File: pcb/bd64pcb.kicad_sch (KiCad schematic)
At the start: 229 parts, among them J1 USB_C_Receptacle_USB2.0, SW1 SW_Push, U1 ATmega32U4-MU, U3 IS31FL3733-QF, Y1 16MHz

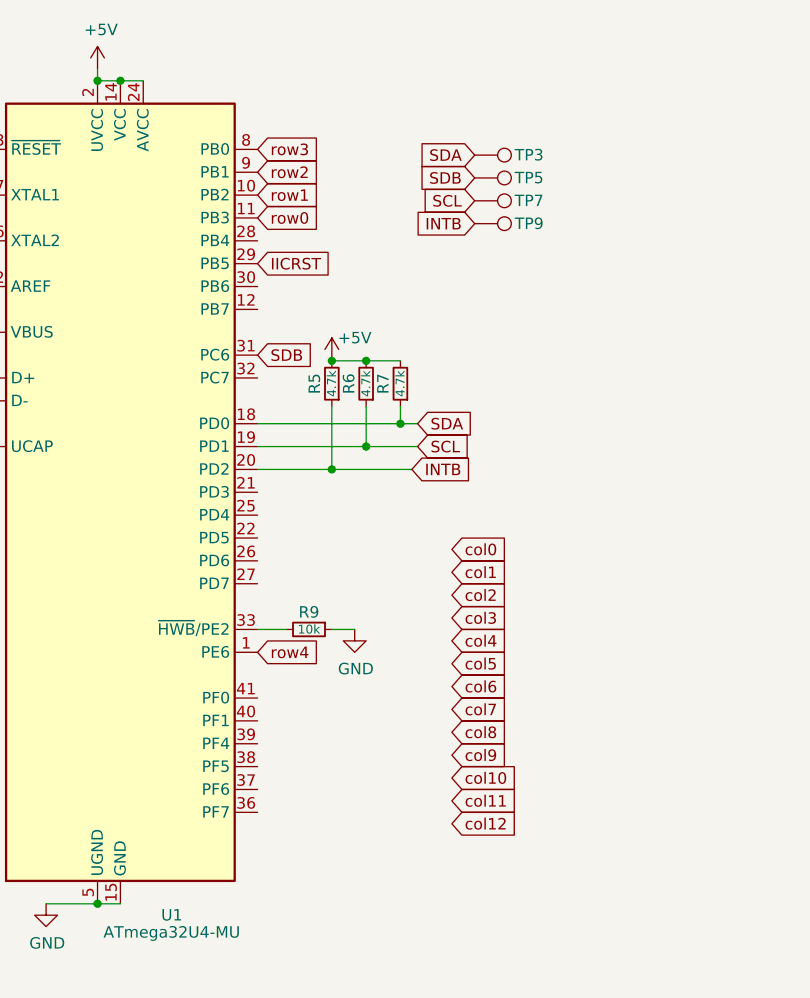
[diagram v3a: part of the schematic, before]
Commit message: rows, cols, and i2c routed
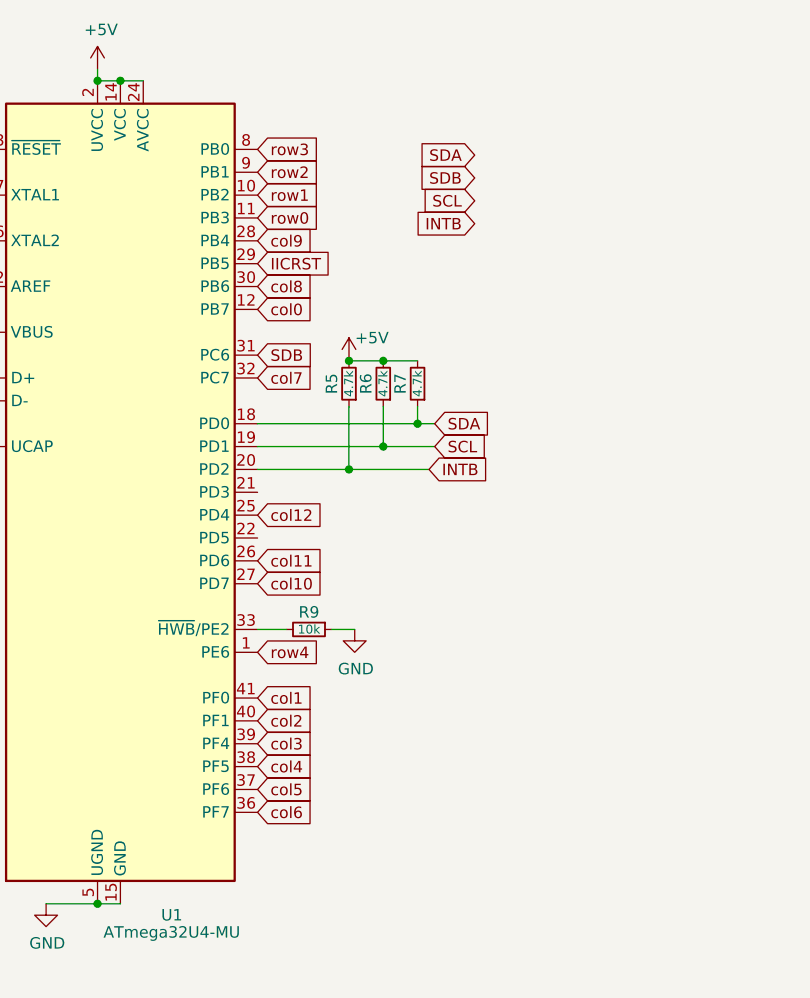
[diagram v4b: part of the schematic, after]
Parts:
- removed TP3, TP5, TP7, TP9: TestPoint, TestPoint:TestPoint_Plated_Hole_D2.0mm, symbol Connector:TestPoint
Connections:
- net col0: now also U1.12 (PB7)
- net col1: now also U1.41 (PF0)
- net col10: now also U1.27 (PD7)
- net col11: now also U1.26 (PD6)
- net col12: now also U1.25 (PD4)
- net col2: now also U1.40 (PF1)
- net col3: now also U1.39 (PF4)
- net col4: now also U1.38 (PF5)
- net col5: now also U1.37 (PF6)
- net col6: now also U1.36 (PF7)
- net col7: now also U1.32 (PC7)
- net col8: now also U1.30 (PB6)
- net col9: now also U1.28 (PB4)
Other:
- moved on the sheet: R5, R6, R7

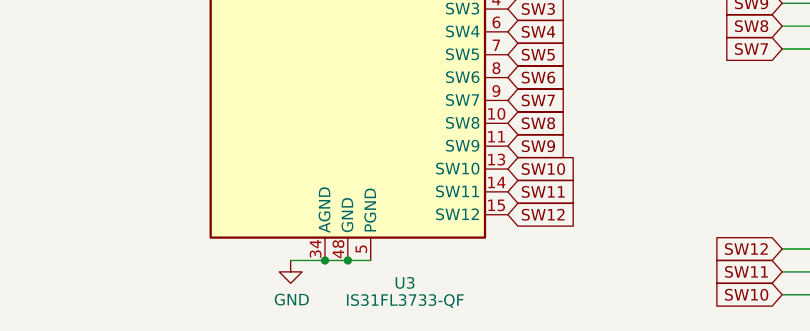
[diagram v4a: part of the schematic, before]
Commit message: decluttering silk labels with arrows
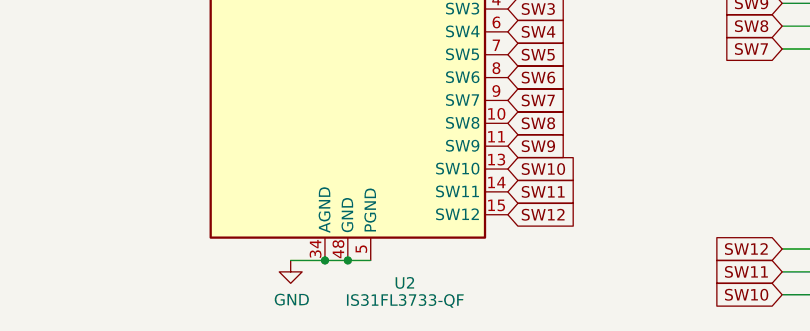
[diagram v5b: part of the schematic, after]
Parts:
- renumbered U3 to U2
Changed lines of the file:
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@@
   (symbol (lib_id "Driver_LED:IS31FL3733-QF") (at 66.675 213.995 0) (unit 1)
     (in_bom yes) (on_board yes)
-    (property "Reference" "U3" (id 0) (at 73.025 257.175 0))
+    (property "Reference" "U2" (id 0) (at 73.025 257.175 0))
     (property "Value" "IS31FL3733-QF" (id 1) (at 73.025 259.08 0))
     (property "Footprint" "Package_DFN_QFN:QFN-48-1EP_6x6mm_P0.4mm_EP4.2x4.2mm" (id 2) (at 66.675 213.995 0)
@@
     )
     (path "/00000000-0000-0000-0000-000062c2eea5"
-      (reference "U3") (unit 1) (value "IS31FL3733-QF") (footprint "Package_DFN_QFN:QFN-48-1EP_6x6mm_P0.4mm_EP4.2x4.2mm")
+      (reference "U2") (unit 1) (value "IS31FL3733-QF") (footprint "Package_DFN_QFN:QFN-48-1EP_6x6mm_P0.4mm_EP4.2x4.2mm")
     )
     (path "/00000000-0000-0000-0000-00006298f3ae"

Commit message: reorg
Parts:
- added J2, J3: Conn_01x04, Connector_JST:JST_SUR_SM04B-SURS-TF_1x04-1MP_P0.80mm_Horizontal, symbol Connector_Generic:Conn_01x04
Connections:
- net +5V: now also J2.2 (Pin_2), J3.2 (Pin_2)
- net GND: now also J2.1 (Pin_1), J2.MP, J3.1 (Pin_1), J3.MP
- net SCL: now also J2.4 (Pin_4), J3.4 (Pin_4)
- net SDA: now also J2.3 (Pin_3), J3.3 (Pin_3)

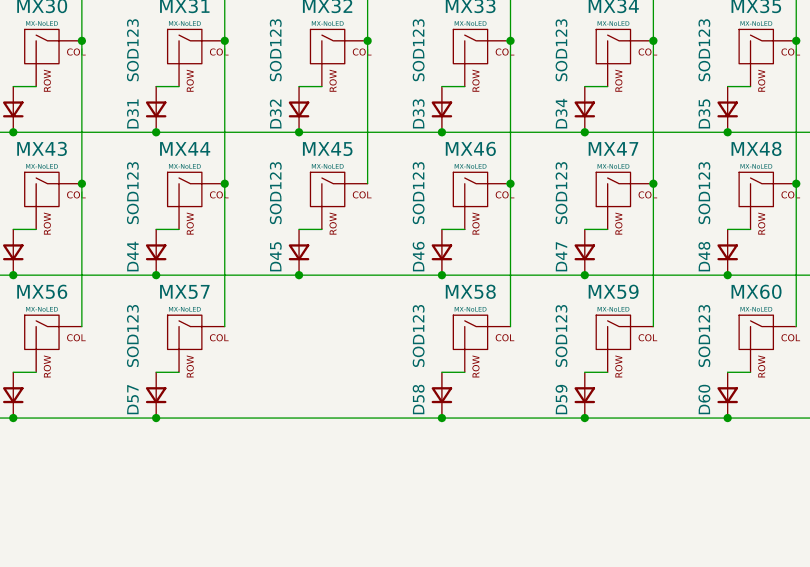
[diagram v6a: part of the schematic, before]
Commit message: update sch footprints, add 6.25 space opt
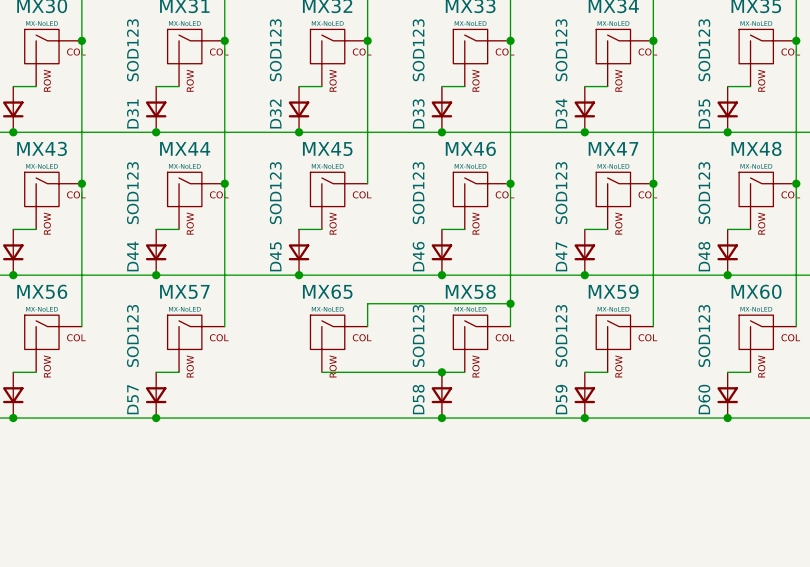
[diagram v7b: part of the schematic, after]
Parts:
- added MX65: MX-NoLED, MX_Only:MXOnly-6.25U-ReversedStabilizers-NoLED, symbol MX_Alps_Hybrid:MX-NoLED
- J1: footprint Connector_USB:USB_C_Receptacle_GCT_USB4085 -> Connector_USB:USB_C_Receptacle_HRO_TYPE-C-31-M-12
- MX10, MX11, MX12, MX13, MX14, MX16, MX17, MX18, MX19, MX20, MX21, MX22, MX23, MX24, MX25, MX26, MX29, MX30, MX31, MX32, MX33, MX34, MX35, MX36, MX37, MX38, MX39, MX4, MX42, MX43, MX44, MX45, MX46, MX47, MX48, MX49, MX5, MX50, MX51, MX52, MX58, MX59, MX6, MX7, MX8, MX9: footprint MX_Alps_Hybrid:MX-1U-NoLED -> MX_Only:MXOnly-1U-NoLED
- MX15, MX53, MX54, MX55, MX61, MX62, MX63, MX64: footprint MX_Alps_Hybrid:MX-1.25U-NoLED -> MX_Only:MXOnly-1.25U-NoLED
- MX27, MX41: footprint MX_Alps_Hybrid:MX-1.75U-NoLED -> MX_Only:MXOnly-1.75U-NoLED
- MX28, MX40, MX56, MX57, MX60: footprint MX_Alps_Hybrid:MX-1.5U-NoLED -> MX_Only:MXOnly-1.5U-NoLED
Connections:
- net col5: now also MX65.1 (COL)
- net at D58.2 (A), MX58.2 (ROW): now also MX65.2 (ROW)

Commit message: scrapping alt space layout
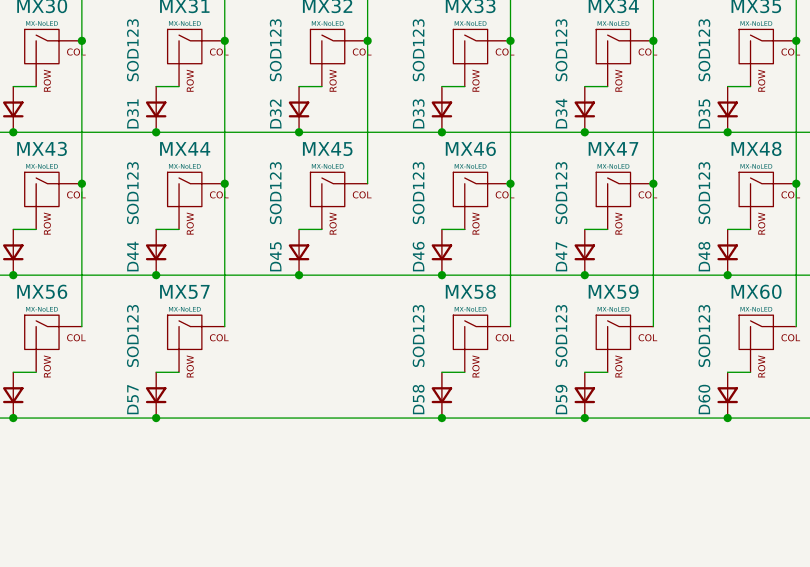
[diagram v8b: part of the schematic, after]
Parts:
- removed MX65: MX-NoLED, MX_Only:MXOnly-6.25U-ReversedStabilizers-NoLED, symbol MX_Alps_Hybrid:MX-NoLED
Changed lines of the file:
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@@
   (junction (at 357.505 60.325) (diameter 0) (color 0 0 0 0)
   )
-  (junction (at 309.88 118.745) (diameter 0) (color 0 0 0 0)
-  )
   (junction (at 262.255 60.325) (diameter 0) (color 0 0 0 0)
   )
@@
   (junction (at 309.88 123.825) (diameter 0) (color 0 0 0 0)
   )
-  (junction (at 317.5 111.125) (diameter 0) (color 0 0 0 0)
-  )
   (junction (at 301.625 171.45) (diameter 0) (color 0 0 0 0)
   )
@@
     (stroke (width 0) (type default) (color 0 0 0 0))
   )
-  (wire (pts (xy 301.625 111.125) (xy 317.5 111.125))
-    (stroke (width 0) (type default) (color 0 0 0 0))
-  )
   (wire (pts (xy 248.92 55.245) (xy 246.38 55.245))
     (stroke (width 0) (type default) (color 0 0 0 0))
@@
     (stroke (width 0) (type default) (color 0 0 0 0))
   )
-  (wire (pts (xy 317.5 113.665) (xy 317.5 111.125))
+  (wire (pts (xy 317.5 97.79) (xy 317.5 113.665))
     (stroke (width 0) (type default) (color 0 0 0 0))
   )
@@
     (stroke (width 0) (type default) (color 0 0 0 0))
   )
-  (wire (pts (xy 301.625 113.665) (xy 301.625 111.125))
-    (stroke (width 0) (type default) (color 0 0 0 0))
-  )
   (wire (pts (xy 81.28 68.58) (xy 77.47 68.58))
     (stroke (width 0) (type default) (color 0 0 0 0))
@@
     (stroke (width 0) (type default) (color 0 0 0 0))
   )
-  (wire (pts (xy 296.545 118.745) (xy 309.88 118.745))
-    (stroke (width 0) (type default) (color 0 0 0 0))
-  )
   (wire (pts (xy 126.365 201.295) (xy 146.05 201.295))
     (stroke (width 0) (type default) (color 0 0 0 0))
@@
     (stroke (width 0) (type default) (color 0 0 0 0))
   )
-  (wire (pts (xy 317.5 111.125) (xy 317.5 97.79))
-    (stroke (width 0) (type default) (color 0 0 0 0))
-  )
   (wire (pts (xy 382.27 201.295) (xy 401.955 201.295))
     (stroke (width 0) (type default) (color 0 0 0 0))
@@
     (pin "1")
   )
-  (symbol (lib_id "MX_Alps_Hybrid:MX-NoLED") (at 297.815 114.935 0) (unit 1)
-    (in_bom yes) (on_board yes)
-    (property "Reference" "MX65" (id 0) (at 297.18 109.855 0)
-      (effects (font (size 1.524 1.524)))
-    )
-    (property "Value" "MX-NoLED" (id 1) (at 297.18 111.76 0)
-      (effects (font (size 0.508 0.508)))
-    )
-    (property "Footprint" "MX_Only:MXOnly-6.25U-ReversedStabilizers-NoLED" (id 2) (at 281.94 115.57 0)
-      (effects (font (size 1.524 1.524)) hide)
-    )
-    (property "Datasheet" "" (id 3) (at 281.94 115.57 0)
-      (effects (font (size 1.524 1.524)) hide)
-    )
-    (pin "1")
-    (pin "2")
-  )
   (symbol (lib_id "Connector_Generic:Conn_01x04") (at 174.625 114.935 0) (unit 1)
     (in_bom yes) (on_board yes) (fields_autoplaced)
@@
       (reference "MX64") (unit 1) (value "MX-NoLED") (footprint "MX_Only:MXOnly-1.25U-NoLED")
     )
-    (path "/762e5ad9-94a3-4764-a6b4-89522ba3b860"
-      (reference "MX65") (unit 1) (value "MX-NoLED") (footprint "MX_Only:MXOnly-6.25U-ReversedStabilizers-NoLED")
-    )
     (path "/00000000-0000-0000-0000-00006c136ea4"
